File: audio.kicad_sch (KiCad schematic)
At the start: 9 parts, among them J4 Conn_01x02, U5 MAX98357A

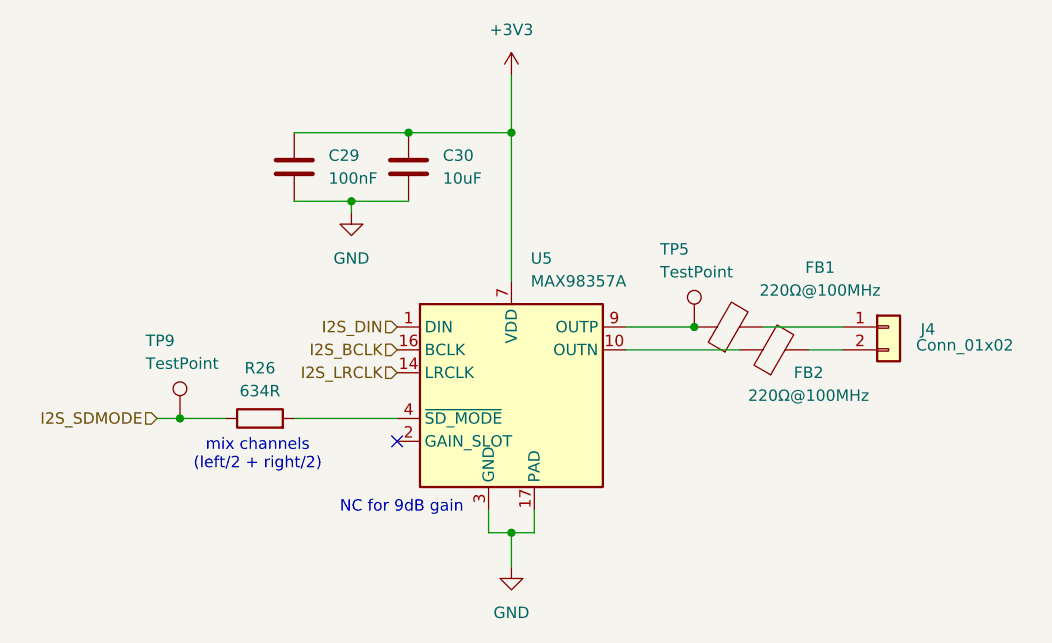
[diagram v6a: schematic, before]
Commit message: proper lcd backlight driver
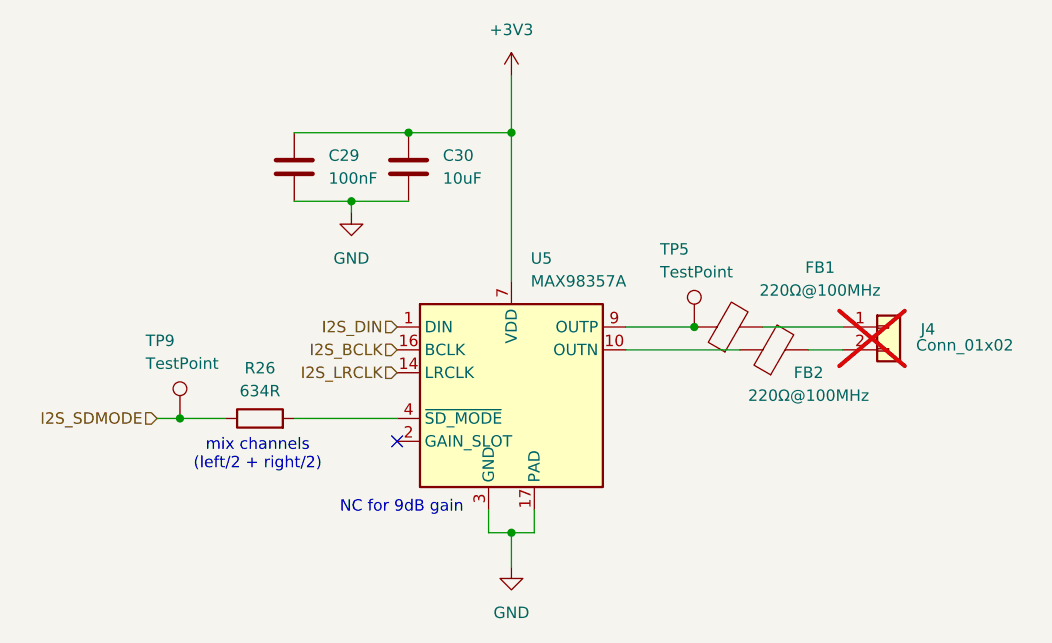
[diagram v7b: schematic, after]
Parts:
- J4: now not fitted; now left out of the parts list
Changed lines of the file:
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@@
 		(unit 1)
 		(exclude_from_sim no)
-		(in_bom yes)
+		(in_bom no)
 		(on_board yes)
-		(dnp no)
+		(dnp yes)
 		(property "Reference" "J4"
 			(at 178.816 91.694 0)

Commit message: changes for production
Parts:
- TP5, TP9: now left out of the parts list
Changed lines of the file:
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@@
 		(unit 1)
 		(exclude_from_sim no)
-		(in_bom yes)
+		(in_bom no)
 		(on_board yes)
 		(dnp no)
@@
 		(unit 1)
 		(exclude_from_sim no)
-		(in_bom yes)
+		(in_bom no)
 		(on_board yes)
 		(dnp no)
